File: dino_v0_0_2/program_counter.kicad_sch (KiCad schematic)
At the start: 18 parts, among them U1 74LS193, U10 74LS04, U11 74LS245, U12 74LS245, U13 74LS245, U14 74LS245, U2 74LS193, U3 74LS193, U4 74LS193

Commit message: Update
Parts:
- removed unit 6 of U10
- added unit 1 of U10
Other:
- moved on the sheet: U10E

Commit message: Schematics WIP
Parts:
- removed unit 1 of U10
- removed unit 2 of U10
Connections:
- no-connect marks 8 -> 4
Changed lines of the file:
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@@
 	)
 	(no_connect
-		(at 81.28 196.85)
-	)
-	(no_connect
-		(at 96.52 196.85)
-	)
-	(no_connect
 		(at 161.29 128.27)
 	)
@@
 	)
 	(no_connect
-		(at 115.57 196.85)
-	)
-	(no_connect
 		(at 119.38 196.85)
 	)
-	(no_connect
-		(at 100.33 196.85)
-	)
 	(bus_entry
 		(at 260.35 44.45)
@@
 	)
 	(symbol
-		(lib_id "74xx:74LS04")
-		(at 88.9 196.85 0)
-		(unit 1)
-		(exclude_from_sim no)
-		(in_bom yes)
-		(on_board yes)
-		(dnp no)
-		(property "Reference" "U10"
-			(at 91.44 191.008 0)
-			(effects
-				(font
-					(size 1.27 1.27)
-				)
-			)
-		)
-		(property "Value" "74LS04"
-			(at 91.44 193.548 0)
-			(effects
-				(font
-					(size 1.27 1.27)
-				)
-			)
-		)
-		(property "Footprint" ""
-			(at 88.9 196.85 0)
-			(effects
-				(font
-					(size 1.27 1.27)
-				)
-				(hide yes)
-			)
-		)
-		(property "Datasheet" "http://www.ti.com/lit/gpn/sn74LS04"
-			(at 88.9 196.85 0)
-			(effects
-				(font
-					(size 1.27 1.27)
-				)
-				(hide yes)
-			)
-		)
-		(property "Description" "Hex Inverter"
-			(at 88.9 196.85 0)
-			(effects
-				(font
-					(size 1.27 1.27)
-				)
-				(hide yes)
-			)
-		)
-		(pin "2"
-		)
-		(pin "3"
-		)
-		(pin "4"
-		)
-		(pin "5"
-		)
-		(pin "6"
-		)
-		(pin "9"
-		)
-		(pin "8"
-		)
-		(pin "11"
-		)
-		(pin "10"
-		)
-		(pin "13"
-		)
-		(pin "12"
-		)
-		(pin "14"
-		)
-		(pin "7"
-		)
-		(pin "1"
-		)
-		(instances
-			(project "dino_v0_0_2"
-				(path "/e43166a5-d972-471d-b3cf-9f4f12c7f541/87747e90-4432-4cdc-a8cb-1da85cd5b65a"
-					(reference "U10")
-					(unit 1)
-				)
-			)
-		)
-	)
-	(symbol
 		(lib_id "Device:C_Small")
 		(at 144.78 105.41 0)
@@
 				)
 			)
-		)
-	)
-	(symbol
-		(lib_id "74xx:74LS04")
-		(at 107.95 196.85 0)
-		(unit 2)
-		(exclude_from_sim no)
-		(in_bom yes)
-		(on_board yes)
-		(dnp no)
-		(property "Reference" "U10"
-			(at 110.49 191.008 0)
-			(effects
-				(font
-					(size 1.27 1.27)
-				)
-			)
-		)
-		(property "Value" "74LS04"
-			(at 110.49 193.548 0)
-			(effects
-				(font
-					(size 1.27 1.27)
-				)
-			)
-		)
-		(property "Footprint" ""
-			(at 107.95 196.85 0)
-			(effects
-				(font
-					(size 1.27 1.27)
-				)
-				(hide yes)
-			)
-		)
-		(property "Datasheet" "http://www.ti.com/lit/gpn/sn74LS04"
-			(at 107.95 196.85 0)
-			(effects
-				(font
-					(size 1.27 1.27)
-				)
-				(hide yes)
-			)
-		)
-		(property "Description" "Hex Inverter"
-			(at 107.95 196.85 0)
-			(effects
-				(font
-					(size 1.27 1.27)
-				)
-				(hide yes)
-			)
-		)
-		(pin "2"
-		)
-		(pin "3"
-		)
-		(pin "4"
-		)
-		(pin "5"
-		)
-		(pin "6"
-		)
-		(pin "9"
-		)
-		(pin "8"
-		)
-		(pin "11"
-		)
-		(pin "10"
-		)
-		(pin "13"
-		)
-		(pin "12"
-		)
-		(pin "14"
-		)
-		(pin "7"
-		)
-		(pin "1"
-		)
-		(instances
-			(project "dino_v0_0_2"
-				(path "/e43166a5-d972-471d-b3cf-9f4f12c7f541/87747e90-4432-4cdc-a8cb-1da85cd5b65a"
-					(reference "U10")
-					(unit 2)
-				)
-			)

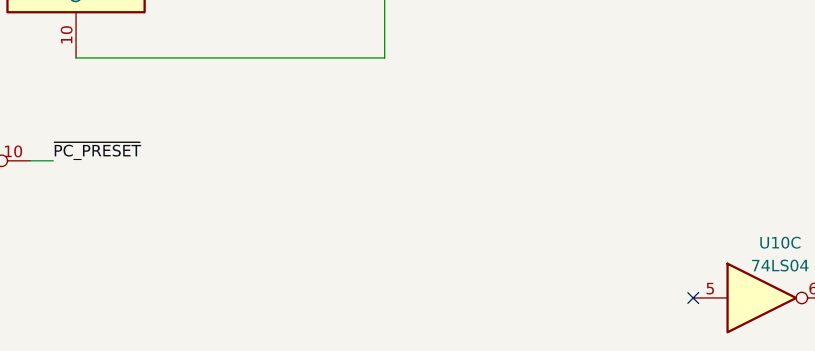
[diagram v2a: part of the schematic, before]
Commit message: Update on Schematics
- Added the 74LS121 to the latches and RAM for intra phase pulses to allow for Latch/Write Enables
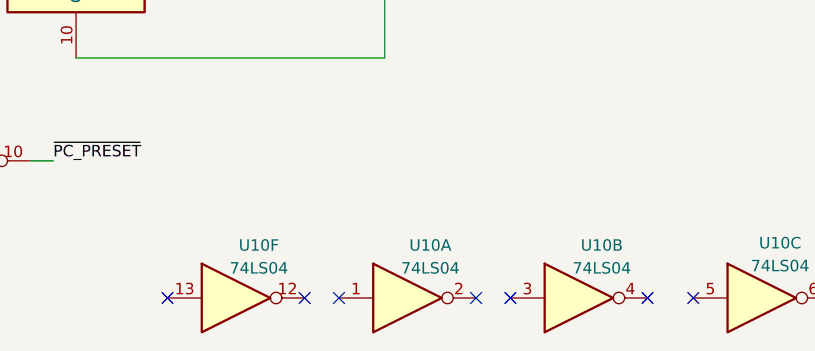
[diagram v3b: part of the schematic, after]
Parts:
- added unit 6 of U10
- added unit 1 of U10
- added unit 2 of U10
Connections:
- no-connect marks 4 -> 10
